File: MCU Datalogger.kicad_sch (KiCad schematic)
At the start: 25 parts, among them U1 24LC1025, U2 24LC1025, U3 DS1337S_T_R, U4 ATMEGA328P-AN, Y1 32.768 KHz, Y2 16 MHz

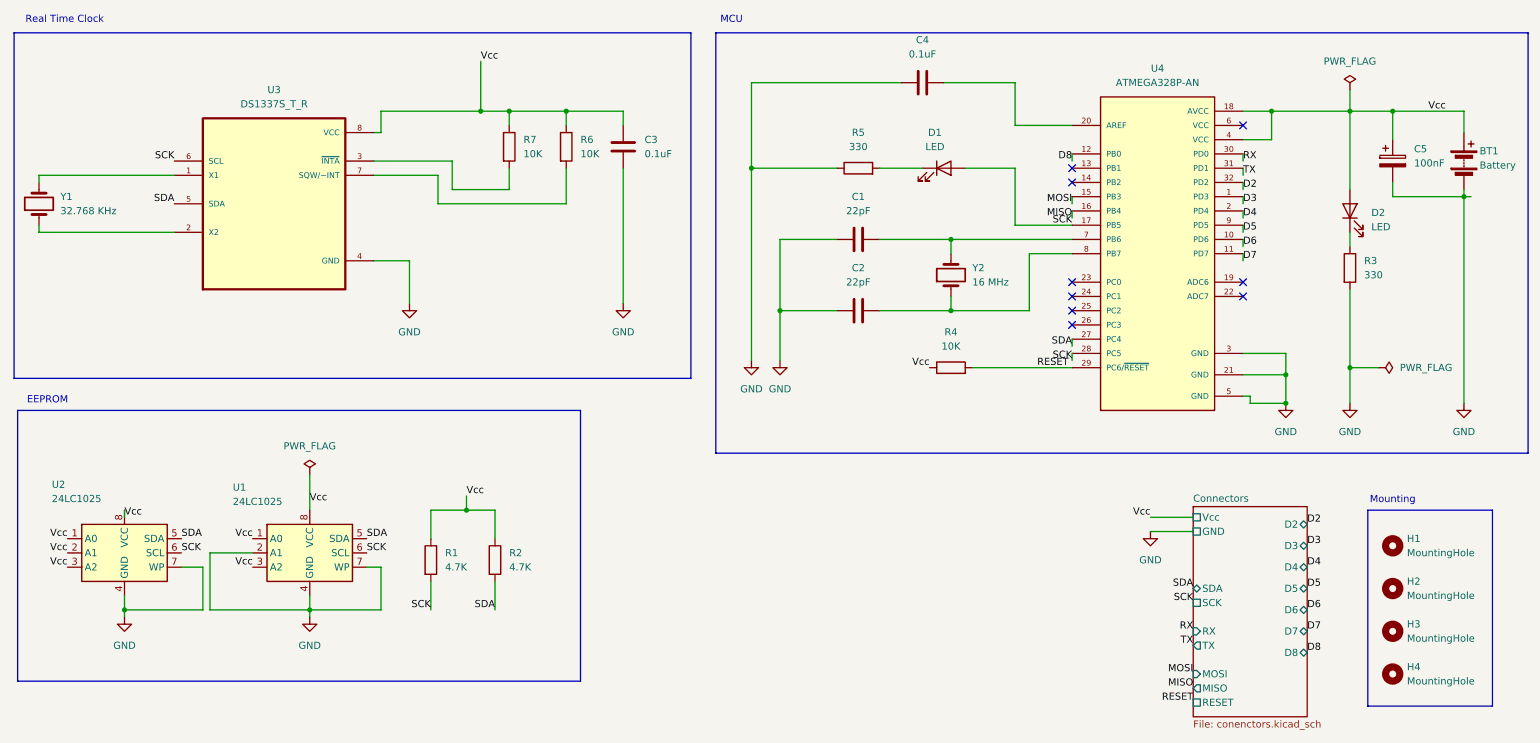
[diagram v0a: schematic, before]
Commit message: fix bug in the schematic with SCK and SCL wires
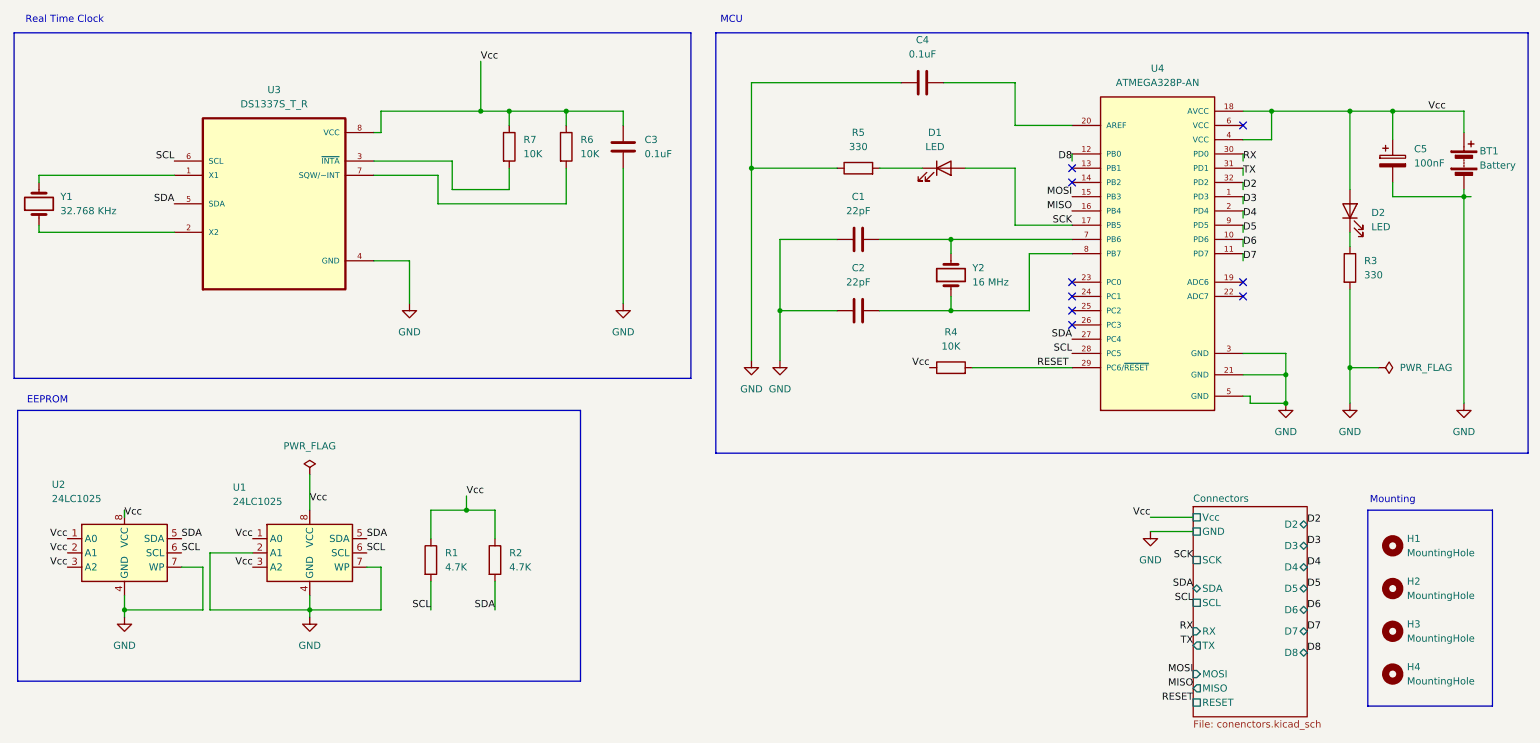
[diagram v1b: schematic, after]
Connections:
- net SCK: no longer R1.2, U1.6 (SCL), U2.6 (SCL), U3.6 (SCL), U4.28 (PC5)
- new net SCL: R1.2, U1.6 (SCL), U2.6 (SCL), U3.6 (SCL), U4.28 (PC5)
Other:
- sheet Connectors ports: added SCL; removed none
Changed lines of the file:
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@@
 	(wire
 		(pts
-			(xy 204.47 73.66) (xy 204.47 74.93)
-		)
-		(stroke
-			(width 0)
-			(type default)
-		)
-	)
-	(wire
-		(pts
 			(xy 236.22 85.09) (xy 242.57 85.09)
 		)
@@
 	(wire
 		(pts
-			(xy 204.47 76.2) (xy 204.47 77.47)
-		)
-		(stroke
-			(width 0)
-			(type default)
-		)
-	)
-	(wire
-		(pts
 			(xy 81.28 114.3) (xy 81.28 121.92)
 		)
@@
 	(wire
 		(pts
-			(xy 204.47 48.26) (xy 204.47 49.53)
-		)
-		(stroke
-			(width 0)
-			(type default)
-		)
-	)
-	(wire
-		(pts
 			(xy 80.01 41.91) (xy 93.98 41.91)
 		)
@@
 	(wire
 		(pts
-			(xy 204.47 50.8) (xy 204.47 52.07)
-		)
-		(stroke
-			(width 0)
-			(type default)
-		)
-	)
-	(wire
-		(pts
 			(xy 204.47 40.64) (xy 204.47 41.91)
 		)
@@
 	(wire
 		(pts
-			(xy 254 33.02) (xy 254 29.21)
-		)
-		(stroke
-			(width 0)
-			(type default)
-		)
-	)
-	(wire
-		(pts
 			(xy 20.32 44.45) (xy 44.45 44.45)
 		)
@@
 		)
 	)
-	(label "SCK"
+	(label "SCL"
 		(at 90.17 121.92 180)
 		(fields_autoplaced yes)
@@
 		)
 	)
-	(label "SCK"
-		(at 204.47 77.47 180)
+	(label "SCL"
+		(at 204.47 76.2 180)
 		(fields_autoplaced yes)
 		(effects
@@
 		)
 	)
-	(label "SCK"
+	(label "SCL"
 		(at 44.45 41.91 180)
 		(fields_autoplaced yes)
@@
 		)
 	)
-	(label "SCK"
+	(label "SCL"
 		(at 45.72 111.76 0)
 		(fields_autoplaced yes)
@@
 		)
 	)
+	(label "SCK"
+		(at 226.06 113.03 180)
+		(fields_autoplaced yes)
+		(effects
+			(font
+				(size 1.27 1.27)
+			)
+			(justify right bottom)
+		)
+	)
 	(label "RX"
 		(at 234.95 41.91 0)
@@
 		)
 	)
-	(label "SCK"
+	(label "SCL"
 		(at 226.06 120.65 180)
 		(fields_autoplaced yes)
@@
 		)
 	)
-	(label "SCK"
+	(label "SCL"
 		(at 78.74 111.76 0)
 		(fields_autoplaced yes)
@@
 	)
 	(label "SDA"
-		(at 204.47 74.93 180)
+		(at 204.47 73.66 180)
 		(fields_autoplaced yes)
 		(effects
@@
 	)
 	(label "MISO"
-		(at 204.47 52.07 180)
+		(at 204.47 50.8 180)
 		(fields_autoplaced yes)
 		(effects
@@
 	)
 	(label "MOSI"
-		(at 204.47 49.53 180)
+		(at 204.47 48.26 180)
 		(fields_autoplaced yes)
 		(effects
@@
 	)
 	(symbol
-		(lib_id "power:PWR_FLAG")
-		(at 254 29.21 0)
-		(unit 1)
-		(exclude_from_sim no)
-		(in_bom yes)
-		(on_board yes)
-		(dnp no)
-		(fields_autoplaced yes)
-		(property "Reference" "#FLG01"
-			(at 254 27.305 0)
-			(effects
-				(font
-					(size 1.27 1.27)
-				)
-				(hide yes)
-			)
-		)
-		(property "Value" "PWR_FLAG"
-			(at 254 24.13 0)
-			(effects
-				(font
-					(size 1.27 1.27)
-				)
-			)
-		)
-		(property "Footprint" ""
-			(at 254 29.21 0)
-			(effects
-				(font
-					(size 1.27 1.27)
-				)
-				(hide yes)
-			)
-		)
-		(property "Datasheet" "~"
-			(at 254 29.21 0)
-			(effects
-				(font
-					(size 1.27 1.27)
-				)
-				(hide yes)
-			)
-		)
-		(property "Description" "Special symbol for telling ERC where power comes from"
-			(at 254 29.21 0)
-			(effects
-				(font
-					(size 1.27 1.27)
-				)
-				(hide yes)
-			)
-		)
-		(pin "1"
-		)
-		(instances
-			(project ""
-				(path "/d838f63e-73b0-481c-88b0-b8875dd02c2f"
-					(reference "#FLG01")
-					(unit 1)
-				)
-			)
-		)
-	)
-	(symbol
 		(lib_id "Device:Crystal")
 		(at 182.88 62.23 90)
@@
 			)
 		)
-		(pin "SCK" passive
-			(at 226.06 120.65 180)
-			(effects
-				(font
-					(size 1.27 1.27)
-				)
-				(justify left)
-			)
-		)
 		(pin "MISO" output
 			(at 226.06 135.89 180)
@@
 			)
 		)
+		(pin "SCL" passive
+			(at 226.06 120.65 180)
+			(effects
+				(font
+					(size 1.27 1.27)
+				)
+				(justify left)
+			)
+		)
+		(pin "SCK" passive
+			(at 226.06 113.03 180)
+			(effects
+				(font
+					(size 1.27 1.27)
+				)
+				(justify left)
+			)
+		)
